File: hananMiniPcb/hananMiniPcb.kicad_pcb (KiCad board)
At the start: 2 copper layers, 83 x 73.2 mm, 19 parts, among them J2 Conn_02x04_Top_Bottom, U1 MCP4901

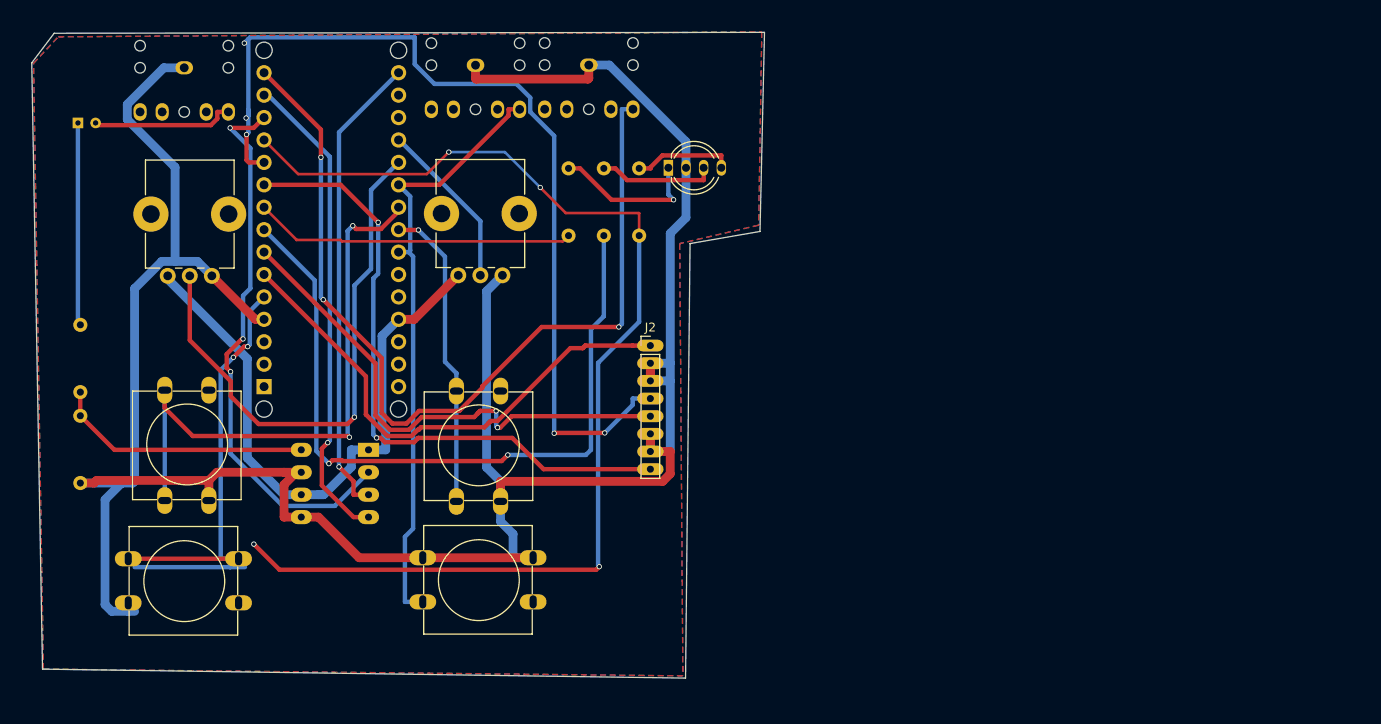
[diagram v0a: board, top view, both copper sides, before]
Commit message: hananMiniPcb v2.0: pads arcade en columna, RC en Vref + 100n en Vdd, pads D1, rótulo de versión
- J2 header 1x08 -> huella ODS:Hanan_PadsArcade_1x08_Pares (8 pads 3.5 mm en columna,
  pares señal/GND, orden blanco/rosa/amarillo/verde), zona GND a toda la placa, M3 como huellas.
- Contorno 150x75 reconstruido del gerber JLC P169.
- R6 1k + C2 10u en Vref (net VREF), C3 100n en Vdd del MCP4901; +5C reruteado.
- Pads de D1 1.25x1.8 (anillo 0.175); stubs/vías colgadas de Pin_4 borrados.
- Title block + silk 'hananMiniPcb ${REVISION} ${ISSUE_DATE}' en F y B.
- docs/revision-electronica-mini.md: revisión eléctrica y alcance de la rev.

Co-Authored-By: Claude Fable 5.1 <noreply@anthropic.com>
Claude-Session: https://claude.ai/code/session_018KSRbDX7mTqiibDixEKAXu
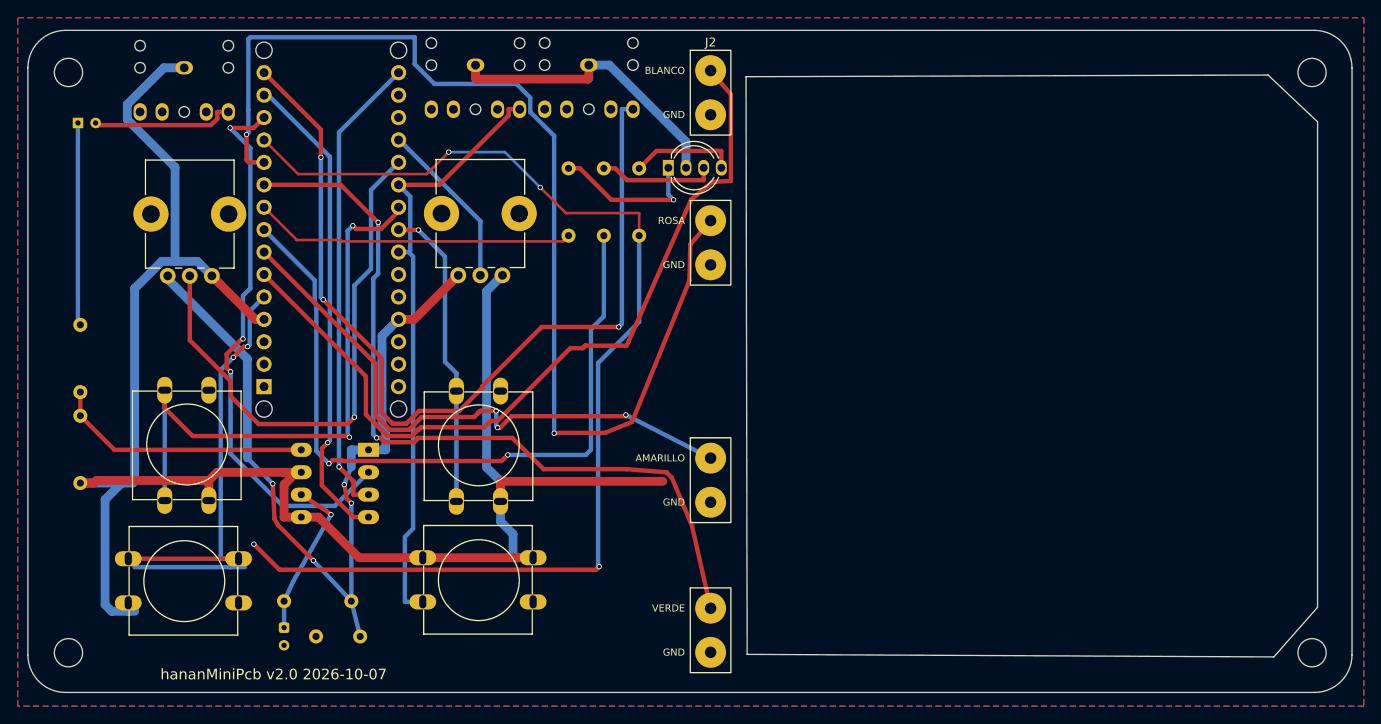
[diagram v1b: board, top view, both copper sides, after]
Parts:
- added C2: 10uF, Capacitor_THT:CP_Radial_D4.0mm_P2.00mm, B.Cu at (79.2, 144.6)
- added C3: 100nF, Capacitor_THT:C_Disc_D5.0mm_W2.5mm_P5.00mm, B.Cu at (87.8, 145.6)
- added H1: MountingHole_3.2mm_M3, MountingHole_3.2mm_M3, F.Cu at (54.8, 81.7)
- added H2: MountingHole_3.2mm_M3, MountingHole_3.2mm_M3, F.Cu at (54.8, 147.4)
- added H3: MountingHole_3.2mm_M3, MountingHole_3.2mm_M3, F.Cu at (195.6, 81.7)
- added H4: MountingHole_3.2mm_M3, MountingHole_3.2mm_M3, F.Cu at (195.6, 147.4)
- added R6: 1k, Resistor_THT:R_Axial_DIN0207_L6.3mm_D2.5mm_P7.62mm_Horizontal, B.Cu at (86.8, 141.6)
- J2: value Conn_02x04_Top_Bottom -> Hanan_PadsArcade_1x08_Pares; footprint Connector_PinHeader_2.00mm:PinHeader_1x08_P2.00mm_Vertical -> Hanan_PadsArcade_1x08_Pares
- moved J2 31.9 mm to (127.5, 81.5)
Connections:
- U1 pad 6: +5C -> VREF
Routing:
- net GND: track 301.2 -> 249.6 mm
- net Net-(J2-Pin_1): track 59.7 -> 93.7 mm
- net +5C: track 69.6 -> 95.4 mm, vias 0 -> 4
- net Net-(J2-Pin_4): track 106.3 -> 125.7 mm, vias 5 -> 2
- net VREF: track 0.00 -> 18.2 mm, vias 0 -> 1
- net Net-(J2-Pin_8): track 72.5 -> 90.7 mm
- net Net-(J2-Pin_5): track 59.2 -> 67.5 mm, vias 2 -> 3
- net Net-(D1-BA): track 11.4 -> 12.0 mm
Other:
- board size 83 x 73.2 mm -> 150 x 75 mm
- board text added: "hananMiniPcb ${REVISION} ${ISSUE_DATE}"
